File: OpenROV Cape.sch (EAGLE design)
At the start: 22 parts, among them IC1 ATMEGA328P-PU, T2 TIP122, T3 2N2222

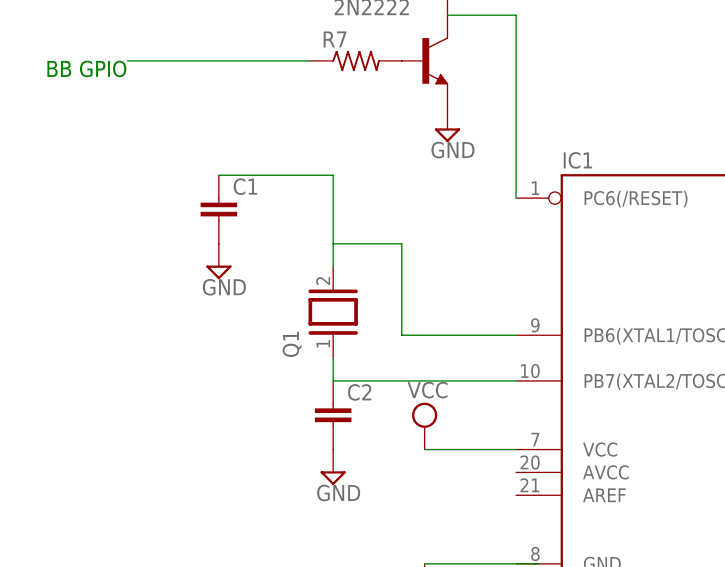
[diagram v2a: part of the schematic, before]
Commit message: swapped out the giant crystal footprint for a smaller standard one with the same hole spacing
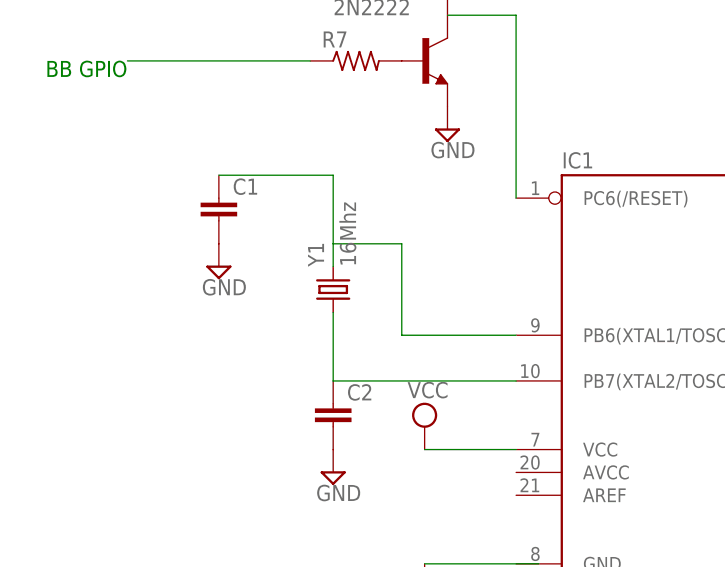
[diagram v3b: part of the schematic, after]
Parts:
- removed Q1: (no value), special:XTAL
- added Y1: 16Mhz, SparkFun:CRYSTALHC49US
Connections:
- net N$24: now also Y1.1; no longer Q1.1
- net N$25: now also Y1.2; no longer Q1.2
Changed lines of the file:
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@@
 <grid distance="0.1" unitdist="inch" unit="inch" style="lines" multiple="1" display="no" altdistance="0.01" altunitdist="inch" altunit="inch"/>
 <layers>
-<layer number="1" name="Top" color="4" fill="1" visible="no" active="no"/>
-<layer number="2" name="Route2" color="1" fill="3" visible="no" active="no"/>
-<layer number="3" name="Route3" color="4" fill="3" visible="no" active="no"/>
-<layer number="4" name="Route4" color="1" fill="4" visible="no" active="no"/>
-<layer number="5" name="Route5" color="4" fill="4" visible="no" active="no"/>
-<layer number="6" name="Route6" color="1" fill="8" visible="no" active="no"/>
-<layer number="7" name="Route7" color="4" fill="8" visible="no" active="no"/>
-<layer number="8" name="Route8" color="1" fill="2" visible="no" active="no"/>
-<layer number="9" name="Route9" color="4" fill="2" visible="no" active="no"/>
-<layer number="10" name="Route10" color="1" fill="7" visible="no" active="no"/>
-<layer number="11" name="Route11" color="4" fill="7" visible="no" active="no"/>
-<layer number="12" name="Route12" color="1" fill="5" visible="no" active="no"/>
-<layer number="13" name="Route13" color="4" fill="5" visible="no" active="no"/>
-<layer number="14" name="Route14" color="1" fill="6" visible="no" active="no"/>
-<layer number="15" name="Route15" color="4" fill="6" visible="no" active="no"/>
-<layer number="16" name="Bottom" color="1" fill="1" visible="no" active="no"/>
-<layer number="17" name="Pads" color="2" fill="1" visible="no" active="no"/>
-<layer number="18" name="Vias" color="2" fill="1" visible="no" active="no"/>
-<layer number="19" name="Unrouted" color="6" fill="1" visible="no" active="no"/>
-<layer number="20" name="Dimension" color="15" fill="1" visible="no" active="no"/>
-<layer number="21" name="tPlace" color="14" fill="1" visible="no" active="no"/>
-<layer number="22" name="bPlace" color="7" fill="1" visible="no" active="no"/>
-<layer number="23" name="tOrigins" color="15" fill="1" visible="no" active="no"/>
-<layer number="24" name="bOrigins" color="15" fill="1" visible="no" active="no"/>
-<layer number="25" name="tNames" color="7" fill="1" visible="no" active="no"/>
-<layer number="26" name="bNames" color="7" fill="1" visible="no" active="no"/>
-<layer number="27" name="tValues" color="7" fill="1" visible="no" active="no"/>
-<layer number="28" name="bValues" color="7" fill="1" visible="no" active="no"/>
+<layer number="1" name="Top" color="4" fill="1" visible="yes" active="no"/>
+<layer number="2" name="Route2" color="1" fill="3" visible="yes" active="no"/>
+<layer number="3" name="Route3" color="4" fill="3" visible="yes" active="no"/>
+<layer number="4" name="Route4" color="1" fill="4" visible="yes" active="no"/>
+<layer number="5" name="Route5" color="4" fill="4" visible="yes" active="no"/>
+<layer number="6" name="Route6" color="1" fill="8" visible="yes" active="no"/>
+<layer number="7" name="Route7" color="4" fill="8" visible="yes" active="no"/>
+<layer number="8" name="Route8" color="1" fill="2" visible="yes" active="no"/>
+<layer number="9" name="Route9" color="4" fill="2" visible="yes" active="no"/>
+<layer number="10" name="Route10" color="1" fill="7" visible="yes" active="no"/>
+<layer number="11" name="Route11" color="4" fill="7" visible="yes" active="no"/>
+<layer number="12" name="Route12" color="1" fill="5" visible="yes" active="no"/>
+<layer number="13" name="Route13" color="4" fill="5" visible="yes" active="no"/>
+<layer number="14" name="Route14" color="1" fill="6" visible="yes" active="no"/>
+<layer number="15" name="Route15" color="4" fill="6" visible="yes" active="no"/>
+<layer number="16" name="Bottom" color="1" fill="1" visible="yes" active="no"/>
+<layer number="17" name="Pads" color="2" fill="1" visible="yes" active="no"/>
+<layer number="18" name="Vias" color="2" fill="1" visible="yes" active="no"/>
+<layer number="19" name="Unrouted" color="6" fill="1" visible="yes" active="no"/>
+<layer number="20" name="Dimension" color="15" fill="1" visible="yes" active="no"/>
+<layer number="21" name="tPlace" color="14" fill="1" visible="yes" active="no"/>
+<layer number="22" name="bPlace" color="7" fill="1" visible="yes" active="no"/>
+<layer number="23" name="tOrigins" color="15" fill="1" visible="yes" active="no"/>
+<layer number="24" name="bOrigins" color="15" fill="1" visible="yes" active="no"/>
+<layer number="25" name="tNames" color="7" fill="1" visible="yes" active="no"/>
+<layer number="26" name="bNames" color="7" fill="1" visible="yes" active="no"/>
+<layer number="27" name="tValues" color="7" fill="1" visible="yes" active="no"/>
+<layer number="28" name="bValues" color="7" fill="1" visible="yes" active="no"/>
 <layer number="29" name="tStop" color="7" fill="3" visible="no" active="no"/>
 <layer number="30" name="bStop" color="7" fill="6" visible="no" active="no"/>
@@
 <layer number="35" name="tGlue" color="7" fill="4" visible="no" active="no"/>
 <layer number="36" name="bGlue" color="7" fill="5" visible="no" active="no"/>
-<layer number="37" name="tTest" color="7" fill="1" visible="no" active="no"/>
-<layer number="38" name="bTest" color="7" fill="1" visible="no" active="no"/>
+<layer number="37" name="tTest" color="7" fill="1" visible="yes" active="no"/>
+<layer number="38" name="bTest" color="7" fill="1" visible="yes" active="no"/>
 <layer number="39" name="tKeepout" color="4" fill="11" visible="no" active="no"/>
 <layer number="40" name="bKeepout" color="1" fill="11" visible="no" active="no"/>
@@
 <layer number="44" name="Drills" color="7" fill="1" visible="no" active="no"/>
 <layer number="45" name="Holes" color="7" fill="1" visible="no" active="no"/>
-<layer number="46" name="Milling" color="3" fill="1" visible="no" active="no"/>
-<layer number="47" name="Measures" color="7" fill="1" visible="no" active="no"/>
-<layer number="48" name="Document" color="7" fill="1" visible="no" active="no"/>
-<layer number="49" name="Reference" color="7" fill="1" visible="no" active="no"/>
-<layer number="50" name="dxf" color="7" fill="1" visible="no" active="no"/>
-<layer number="51" name="tDocu" color="7" fill="1" visible="no" active="no"/>
-<layer number="52" name="bDocu" color="7" fill="1" visible="no" active="no"/>
-<layer number="53" name="tGND_GNDA" color="7" fill="9" visible="no" active="no"/>
-<layer number="54" name="bGND_GNDA" color="1" fill="9" visible="no" active="no"/>
-<layer number="56" name="wert" color="7" fill="1" visible="no" active="no"/>
+<layer number="46" name="Milling" color="3" fill="1" visible="yes" active="no"/>
+<layer number="47" name="Measures" color="7" fill="1" visible="yes" active="no"/>
+<layer number="48" name="Document" color="7" fill="1" visible="yes" active="no"/>
+<layer number="49" name="Reference" color="7" fill="1" visible="yes" active="no"/>
+<layer number="50" name="dxf" color="7" fill="1" visible="yes" active="no"/>
+<layer number="51" name="tDocu" color="7" fill="1" visible="yes" active="no"/>
+<layer number="52" name="bDocu" color="7" fill="1" visible="yes" active="no"/>
+<layer number="53" name="tGND_GNDA" color="7" fill="9" visible="yes" active="no"/>
+<layer number="54" name="bGND_GNDA" color="1" fill="9" visible="yes" active="no"/>
+<layer number="56" name="wert" color="7" fill="1" visible="yes" active="no"/>
 <layer number="91" name="Nets" color="2" fill="1" visible="yes" active="yes"/>
 <layer number="92" name="Busses" color="1" fill="1" visible="yes" active="yes"/>
@@
 <part name="R2" library="rcl" deviceset="R-US_" device="0204/7"/>
 <part name="SUPPLY4" library="supply2" deviceset="GND" device=""/>
-<part name="Q1" library="special" deviceset="XTAL" device=""/>
 <part name="C1" library="capacitor-wima" deviceset="C" device="2,5-3"/>
 <part name="C2" library="capacitor-wima" deviceset="C" device="2,5-3"/>
@@
 <part name="R7" library="rcl" deviceset="R-US_" device="0204/7"/>
 <part name="SUPPLY21" library="supply2" deviceset="VCC" device=""/>
+<part name="Y1" library="SparkFun" deviceset="CRYSTAL" device="HC49US" value="16Mhz"/>
 </parts>
 <sheets>
@@
 <instance part="R2" gate="G$1" x="142.24" y="53.34"/>
 <instance part="SUPPLY4" gate="GND" x="137.16" y="38.1"/>
-<instance part="Q1" gate="G$1" x="55.88" y="60.96" rot="R90"/>
 <instance part="C1" gate="G$1" x="43.18" y="73.66"/>
 <instance part="C2" gate="G$1" x="55.88" y="50.8"/>
@@
 <instance part="R7" gate="G$1" x="58.42" y="88.9"/>
 <instance part="SUPPLY21" gate="G$1" x="68.58" y="106.68"/>
+<instance part="Y1" gate="G$1" x="55.88" y="63.5" rot="R90"/>
 </instances>
 <busses>
@@
 <net name="N$24" class="0">
 <segment>
-<pinref part="Q1" gate="G$1" pin="1"/>
 <pinref part="C2" gate="G$1" pin="1"/>
-<wire x1="55.88" y1="53.34" x2="55.88" y2="55.88" width="0.1524" layer="91"/>
 <pinref part="IC1" gate="G$1" pin="PB7(XTAL2/TOSC2)"/>
 <wire x1="55.88" y1="53.34" x2="76.2" y2="53.34" width="0.1524" layer="91"/>
+<pinref part="Y1" gate="G$1" pin="1"/>
+<wire x1="55.88" y1="53.34" x2="55.88" y2="60.96" width="0.1524" layer="91"/>
 </segment>
 </net>
 <net name="N$25" class="0">
 <segment>
-<wire x1="55.88" y1="66.04" x2="55.88" y2="68.58" width="0.1524" layer="91"/>
 <wire x1="55.88" y1="68.58" x2="55.88" y2="76.2" width="0.1524" layer="91"/>
 <wire x1="55.88" y1="76.2" x2="43.18" y2="76.2" width="0.1524" layer="91"/>
-<pinref part="Q1" gate="G$1" pin="2"/>
 <pinref part="C1" gate="G$1" pin="1"/>
 <pinref part="IC1" gate="G$1" pin="PB6(XTAL1/TOSC1)"/>
@@
 <wire x1="63.5" y1="58.42" x2="63.5" y2="68.58" width="0.1524" layer="91"/>
 <wire x1="63.5" y1="68.58" x2="55.88" y2="68.58" width="0.1524" layer="91"/>
-</segment>
-</net>
+<pinref part="Y1" gate="G$1" pin="2"/>
+<wire x1="55.88" y1="66.04" x2="55.88" y2="68.58" width="0.1524" layer="91"/>
+</segment>
+</net>

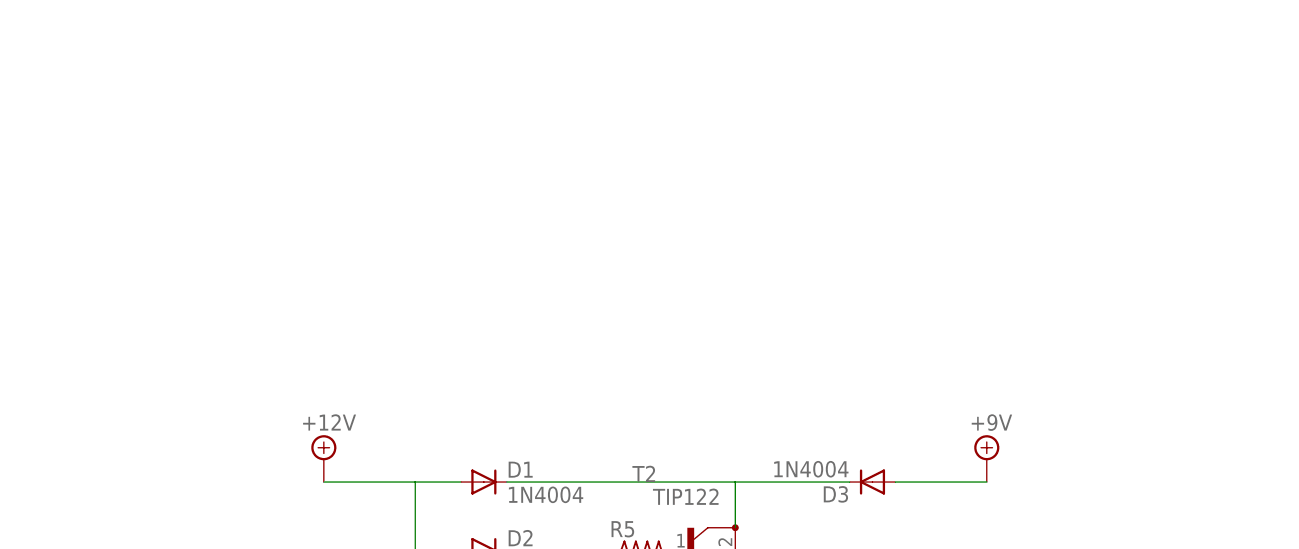
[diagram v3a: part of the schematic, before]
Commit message: added headers for +9V and +12V
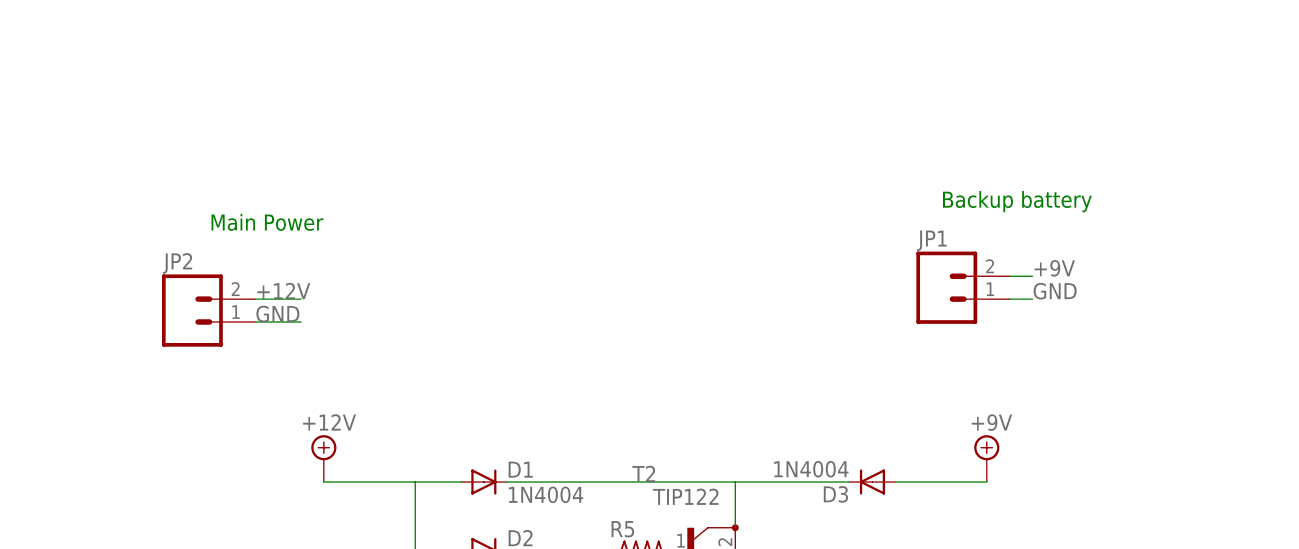
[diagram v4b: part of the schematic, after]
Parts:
- added JP1, JP2: (no value), SparkFun:M02PTH
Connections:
- net +12V: now also JP2.2
- net +9V: now also JP1.2
- net GND: now also JP1.1, JP2.1
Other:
- note added: "Backup battery"
- note added: "Main Power"
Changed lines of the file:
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@@
 <part name="SUPPLY21" library="supply2" deviceset="VCC" device=""/>
 <part name="Y1" library="SparkFun" deviceset="CRYSTAL" device="HC49US" value="16Mhz"/>
+<part name="JP1" library="SparkFun" deviceset="M02" device="PTH"/>
+<part name="JP2" library="SparkFun" deviceset="M02" device="PTH"/>
 </parts>
 <sheets>
@@
 <text x="170.18" y="121.92" size="1.778" layer="91" rot="R180">Starbord ESC</text>
 <text x="33.02" y="88.9" size="1.778" layer="91" rot="R180">BB GPIO</text>
+<text x="200.66" y="228.6" size="1.778" layer="91">Backup battery</text>
+<text x="119.38" y="226.06" size="1.778" layer="91">Main Power</text>
 </plain>
 <instances>
@@
 <instance part="SUPPLY21" gate="G$1" x="68.58" y="106.68"/>
 <instance part="Y1" gate="G$1" x="55.88" y="63.5" rot="R90"/>
+<instance part="JP1" gate="G$1" x="200.66" y="218.44"/>
+<instance part="JP2" gate="G$1" x="116.84" y="215.9"/>
 </instances>
 <busses>
@@
 <wire x1="66.04" y1="33.02" x2="78.74" y2="33.02" width="0.1524" layer="91"/>
 </segment>
+<segment>
+<pinref part="JP2" gate="G$1" pin="1"/>
+<wire x1="124.46" y1="215.9" x2="129.54" y2="215.9" width="0.1524" layer="91"/>
+<label x="124.46" y="215.9" size="1.778" layer="95"/>
+</segment>
+<segment>
+<pinref part="JP1" gate="G$1" pin="1"/>
+<wire x1="208.28" y1="218.44" x2="210.82" y2="218.44" width="0.1524" layer="91"/>
+<label x="210.82" y="218.44" size="1.778" layer="95"/>
+</segment>
 </net>
 <net name="N$24" class="0">
@@
 <pinref part="SUPPLY11" gate="G$1" pin="+9V"/>
 </segment>
+<segment>
+<pinref part="JP1" gate="G$1" pin="2"/>
+<wire x1="208.28" y1="220.98" x2="210.82" y2="220.98" width="0.1524" layer="91"/>
+<label x="210.82" y="220.98" size="1.778" layer="95"/>
+</segment>
 </net>
 <net name="+12V" class="0">
@@
 <pinref part="SUPPLY12" gate="+12V" pin="+12V"/>
 </segment>
-</net>
+<segment>
+<pinref part="JP2" gate="G$1" pin="2"/>
+<wire x1="124.46" y1="218.44" x2="129.54" y2="218.44" width="0.1524" layer="91"/>
+<label x="124.46" y="218.44" size="1.778" layer="95"/>
+</segment>
+</net>
